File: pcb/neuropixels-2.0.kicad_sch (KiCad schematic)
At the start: 12 parts, among them J2 FH35C-17S-0.3SHW(99), J3 FH35C-17S-0.3SHW(99), U4 STG3856, U5 ECS-2016MV-480-CN-TR

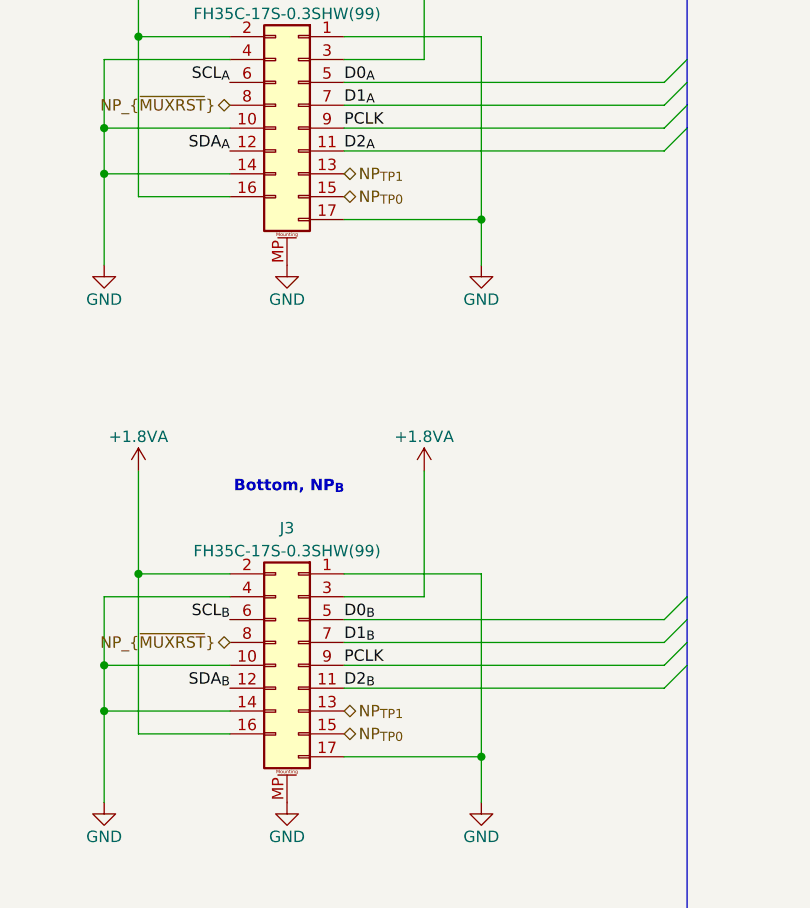
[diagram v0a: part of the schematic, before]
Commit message: Rev. A of public version of headstage
- Being fabricated for testing
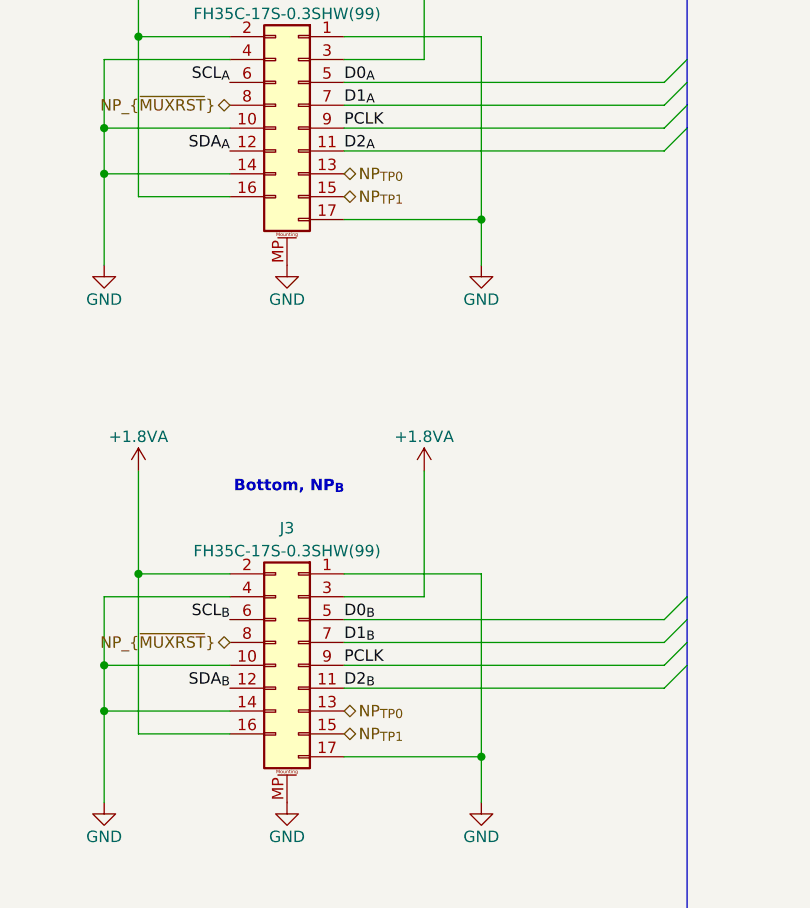
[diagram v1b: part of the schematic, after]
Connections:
- net NP_{TP0}: now also J2.13 (Pin_13), J3.13 (Pin_13); no longer J2.15 (Pin_15), J3.15 (Pin_15)
- net NP_{TP1}: now also J2.15 (Pin_15), J3.15 (Pin_15); no longer J2.13 (Pin_13), J3.13 (Pin_13)
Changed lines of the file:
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@@
   (title_block
     (title "ONIX Neuropixels 2.0 Economical Headstage")
-    (rev "B")
+    (rev "A")
     (company "Open Ephys, Inc")
     (comment 1 "Jonathan P. Newman")
@@
     (effects (font (size 1.27 1.27)) (justify left bottom))
   )
-  (hierarchical_label "NP_{TP1}" (shape bidirectional) (at 176.53 109.22 0) (fields_autoplaced)
+  (hierarchical_label "NP_{TP0}" (shape bidirectional) (at 176.53 49.53 0) (fields_autoplaced)
+    (effects (font (size 1.27 1.27)) (justify left))
+  )
+  (hierarchical_label "NP_{TP1}" (shape bidirectional) (at 176.53 52.07 0) (fields_autoplaced)
     (effects (font (size 1.27 1.27)) (justify left))
   )
   (hierarchical_label "{PSB}" (shape bidirectional) (at 218.44 29.21 0) (fields_autoplaced)
-    (effects (font (size 1.27 1.27)) (justify left))
-  )
-  (hierarchical_label "NP_{TP0}" (shape bidirectional) (at 176.53 111.76 0) (fields_autoplaced)
     (effects (font (size 1.27 1.27)) (justify left))
   )
@@
     (effects (font (size 1.27 1.27)) (justify right))
   )
-  (hierarchical_label "NP_{TP1}" (shape bidirectional) (at 176.53 49.53 0) (fields_autoplaced)
+  (hierarchical_label "NP_{TP1}" (shape bidirectional) (at 176.53 111.76 0) (fields_autoplaced)
     (effects (font (size 1.27 1.27)) (justify left))
   )
@@
     (effects (font (size 1.27 1.27)) (justify right))
   )
-  (hierarchical_label "NP_{TP0}" (shape bidirectional) (at 176.53 52.07 0) (fields_autoplaced)
-    (effects (font (size 1.27 1.27)) (justify left))
-  )
+  (hierarchical_label "NP_{TP0}" (shape bidirectional) (at 176.53 109.22 0) (fields_autoplaced)
+    (effects (font (size 1.27 1.27)) (justify left))
+  )

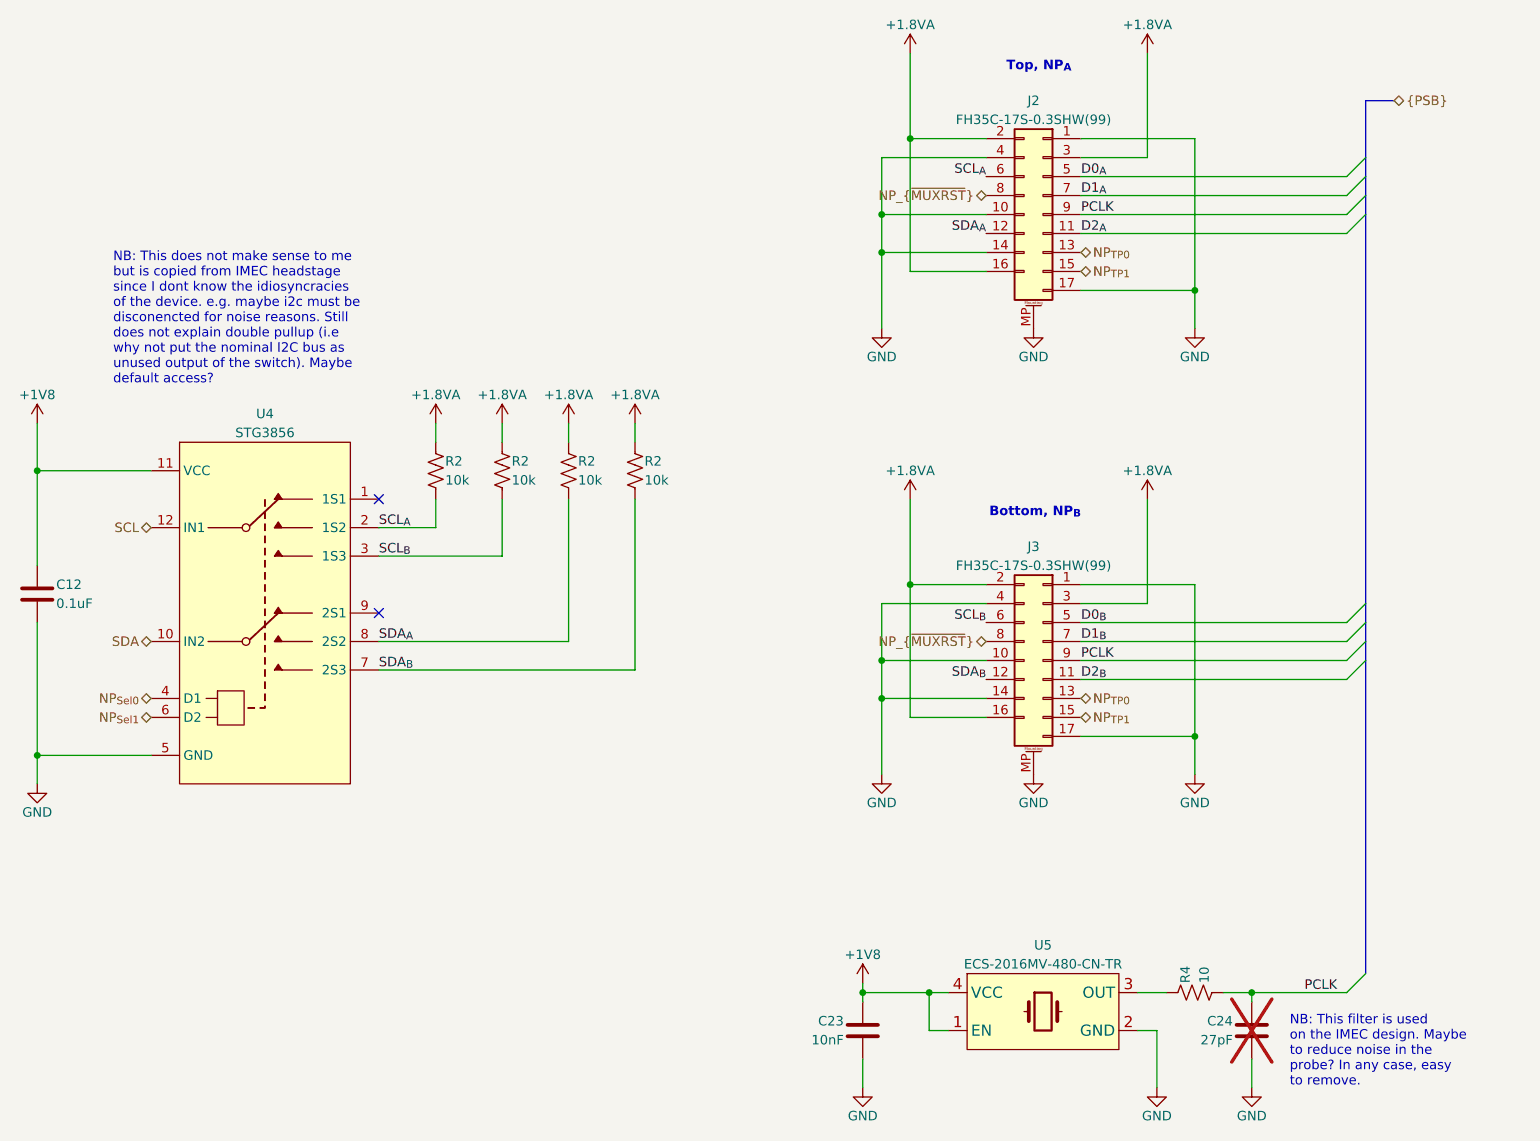
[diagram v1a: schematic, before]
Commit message: Revision B
- Fix incorrect STG3856 symbol and make corresponding changes to PCB
- Flip bits 1 and 2 in probe interaces (fixes #1)
- Improve silkscreen
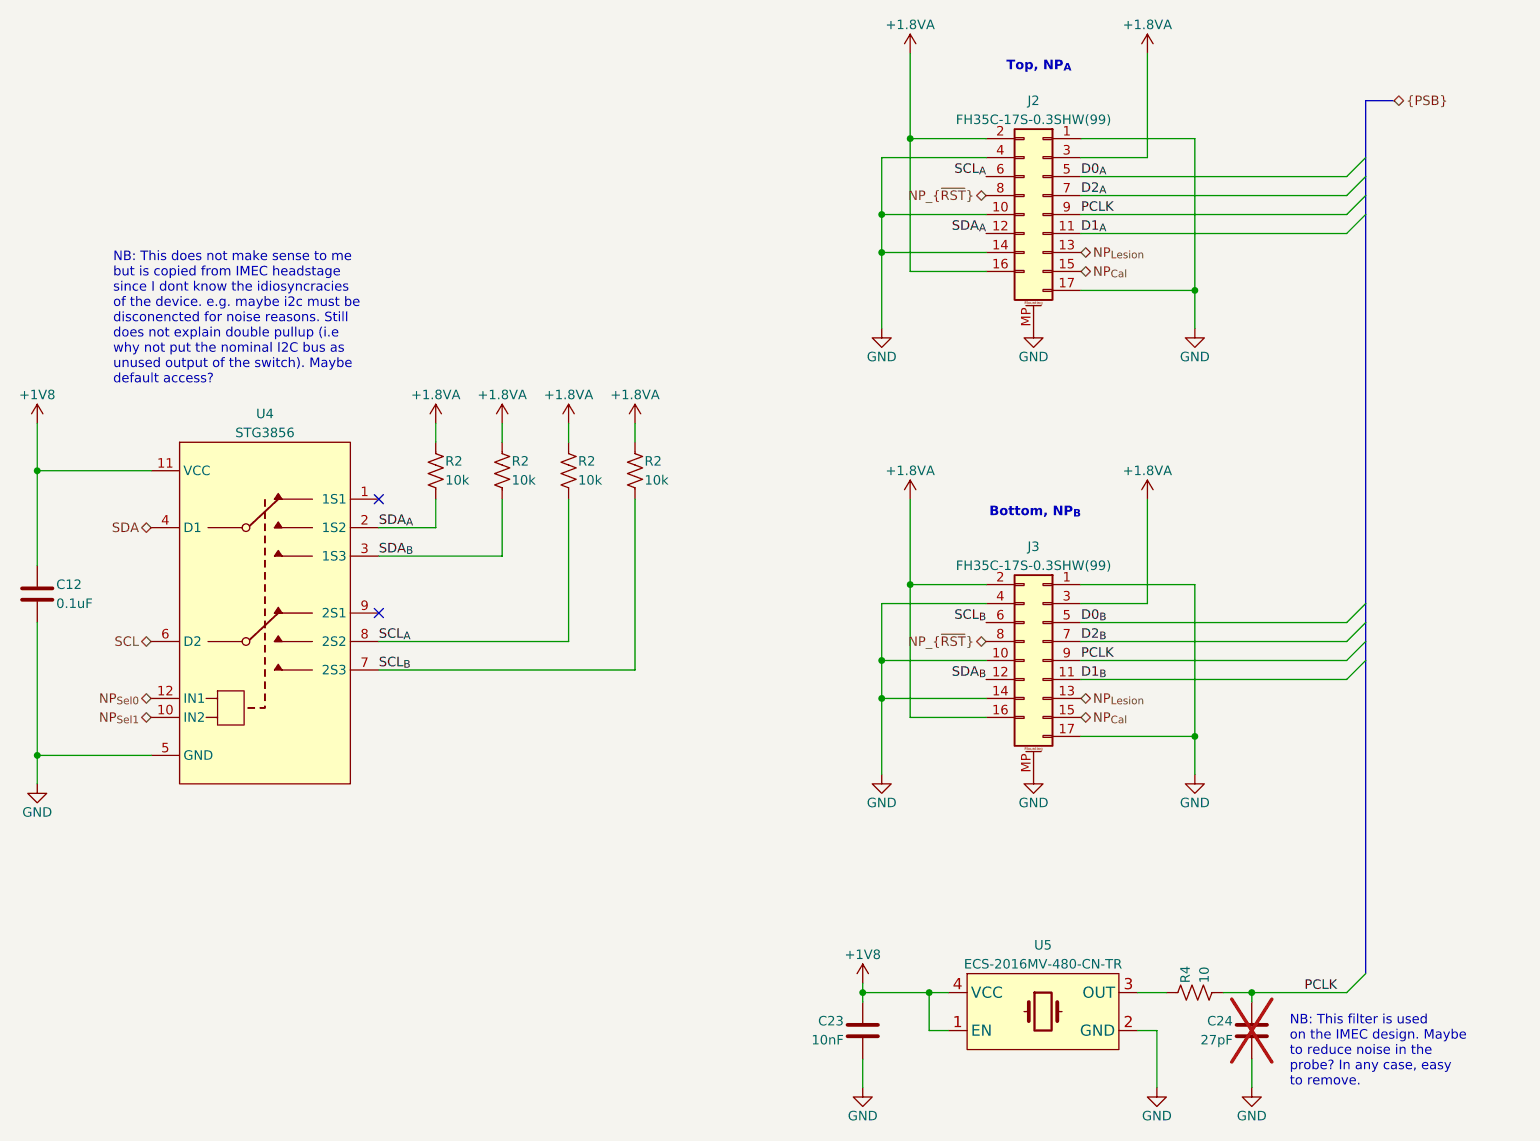
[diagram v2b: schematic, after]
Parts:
- C12, C23, C24, J2, J3, R2, R4, U5: OEPS PN (none) -> ??
- U4: symbol jonnew:STG3856 -> open-ephys:STG3856; OEPS PN (none) -> ??
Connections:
- net D1_{A}: now also J2.11 (Pin_11); no longer J2.7 (Pin_7)
- net D1_{B}: now also J3.11 (Pin_11); no longer J3.7 (Pin_7)
- net D2_{A}: now also J2.7 (Pin_7); no longer J2.11 (Pin_11)
- net D2_{B}: now also J3.7 (Pin_7); no longer J3.11 (Pin_11)
- net NP_{Sel0}: now also U4.12 (IN1); no longer U4.4 (D1)
- net NP_{Sel1}: now also U4.10 (IN2); no longer U4.6 (D2)
- net SCL: now also U4.6 (D2); no longer U4.12 (IN1)
- net SCL_{A}: now also R2.2, U4.8 (2S2); no longer R2.2, U4.2 (1S2)
- net SCL_{B}: now also R2.2, U4.7 (2S3); no longer R2.2, U4.3 (1S3)
- net SDA: now also U4.4 (D1); no longer U4.10 (IN2)
- net SDA_{A}: now also R2.2, U4.2 (1S2); no longer R2.2, U4.8 (2S2)
- net SDA_{B}: now also R2.2, U4.3 (1S3); no longer R2.2, U4.7 (2S3)
- net NP_{TP0} renamed NP_{Lesion}
- net NP_{TP1} renamed NP_{Cal}
- net NP_{~{MUXRST}} renamed NP_{~{RST}}
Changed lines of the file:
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@@
   (title_block
     (title "ONIX Neuropixels 2.0 Economical Headstage")
-    (rev "A")
+    (rev "B")
     (company "Open Ephys, Inc")
     (comment 1 "Jonathan P. Newman")
@@
     (effects (font (size 1.27 1.27)) (justify left bottom))
   )
-  (label "D2_{B}" (at 176.53 106.68 0) (fields_autoplaced)
+  (label "SCL_{A}" (at 82.55 101.6 0) (fields_autoplaced)
     (effects (font (size 1.27 1.27)) (justify left bottom))
   )
-  (label "SCL_{A}" (at 82.55 86.36 0) (fields_autoplaced)
+  (label "D1_{B}" (at 176.53 106.68 0) (fields_autoplaced)
     (effects (font (size 1.27 1.27)) (justify left bottom))
   )
-  (label "SDA_{A}" (at 82.55 101.6 0) (fields_autoplaced)
+  (label "SCL_{B}" (at 82.55 105.41 0) (fields_autoplaced)
     (effects (font (size 1.27 1.27)) (justify left bottom))
   )
@@
     (effects (font (size 1.27 1.27)) (justify left bottom))
   )
+  (label "SDA_{A}" (at 82.55 86.36 0) (fields_autoplaced)
+    (effects (font (size 1.27 1.27)) (justify left bottom))
+  )
   (label "SCL_{A}" (at 163.83 39.37 180) (fields_autoplaced)
     (effects (font (size 1.27 1.27)) (justify right bottom))
@@
     (effects (font (size 1.27 1.27)) (justify left bottom))
   )
-  (label "SCL_{B}" (at 82.55 90.17 0) (fields_autoplaced)
+  (label "SDA_{B}" (at 82.55 90.17 0) (fields_autoplaced)
     (effects (font (size 1.27 1.27)) (justify left bottom))
   )
@@
     (effects (font (size 1.27 1.27)) (justify right bottom))
   )
-  (label "D1_{A}" (at 176.53 41.91 0) (fields_autoplaced)
-    (effects (font (size 1.27 1.27)) (justify left bottom))
-  )
-  (label "SDA_{B}" (at 82.55 105.41 0) (fields_autoplaced)
+  (label "D2_{A}" (at 176.53 41.91 0) (fields_autoplaced)
     (effects (font (size 1.27 1.27)) (justify left bottom))
   )
@@
     (effects (font (size 1.27 1.27)) (justify left bottom))
   )
-  (label "D1_{B}" (at 176.53 101.6 0) (fields_autoplaced)
+  (label "D2_{B}" (at 176.53 101.6 0) (fields_autoplaced)
     (effects (font (size 1.27 1.27)) (justify left bottom))
   )
@@
     (effects (font (size 1.27 1.27)) (justify right bottom))
   )
-  (label "D2_{A}" (at 176.53 46.99 0) (fields_autoplaced)
+  (label "D1_{A}" (at 176.53 46.99 0) (fields_autoplaced)
     (effects (font (size 1.27 1.27)) (justify left bottom))
   )
-  (hierarchical_label "NP_{TP0}" (shape bidirectional) (at 176.53 49.53 0) (fields_autoplaced)
+  (hierarchical_label "NP_{Lesion}" (shape bidirectional) (at 176.53 49.53 0) (fields_autoplaced)
     (effects (font (size 1.27 1.27)) (justify left))
   )
-  (hierarchical_label "NP_{TP1}" (shape bidirectional) (at 176.53 52.07 0) (fields_autoplaced)
+  (hierarchical_label "NP_{Cal}" (shape bidirectional) (at 176.53 52.07 0) (fields_autoplaced)
     (effects (font (size 1.27 1.27)) (justify left))
+  )
+  (hierarchical_label "SCL" (shape bidirectional) (at 52.07 101.6 180) (fields_autoplaced)
+    (effects (font (size 1.27 1.27)) (justify right))
   )
   (hierarchical_label "{PSB}" (shape bidirectional) (at 218.44 29.21 0) (fields_autoplaced)
     (effects (font (size 1.27 1.27)) (justify left))
   )
-  (hierarchical_label "SDA" (shape bidirectional) (at 52.07 101.6 180) (fields_autoplaced)
+  (hierarchical_label "NP_{Cal}" (shape bidirectional) (at 176.53 111.76 0) (fields_autoplaced)
+    (effects (font (size 1.27 1.27)) (justify left))
+  )
+  (hierarchical_label "NP_{~{RST}}" (shape bidirectional) (at 163.83 41.91 180) (fields_autoplaced)
     (effects (font (size 1.27 1.27)) (justify right))
   )
-  (hierarchical_label "NP_{TP1}" (shape bidirectional) (at 176.53 111.76 0) (fields_autoplaced)
+  (hierarchical_label "NP_{Lesion}" (shape bidirectional) (at 176.53 109.22 0) (fields_autoplaced)
     (effects (font (size 1.27 1.27)) (justify left))
   )
-  (hierarchical_label "NP_{~{MUXRST}}" (shape bidirectional) (at 163.83 41.91 180) (fields_autoplaced)
+  (hierarchical_label "SDA" (shape bidirectional) (at 52.07 86.36 180) (fields_autoplaced)
     (effects (font (size 1.27 1.27)) (justify right))
   )
-  (hierarchical_label "SCL" (shape bidirectional) (at 52.07 86.36 180) (fields_autoplaced)
-    (effects (font (size 1.27 1.27)) (justify right))
-  )
-  (hierarchical_label "NP_{TP0}" (shape bidirectional) (at 176.53 109.22 0) (fields_autoplaced)
-    (effects (font (size 1.27 1.27)) (justify left))
-  )
-  (hierarchical_label "NP_{~{MUXRST}}" (shape bidirectional) (at 163.83 101.6 180) (fields_autoplaced)
+  (hierarchical_label "NP_{~{RST}}" (shape bidirectional) (at 163.83 101.6 180) (fields_autoplaced)
     (effects (font (size 1.27 1.27)) (justify right))
   )
@@
     )
   )
-  (symbol (lib_id "jonnew:STG3856") (at 67.31 97.79 0) (unit 1)
+  (symbol (lib_id "open-ephys:STG3856") (at 67.31 97.79 0) (unit 1)
     (in_bom yes) (on_board yes) (dnp no) (fields_autoplaced)
     (property "Reference" "U4" (at 67.31 71.12 0)
@@
     )
     (property "Datasheet" "https://www.st.com/resource/en/datasheet/stg3856.pdf" (at 67.31 97.79 0)
+      (effects (font (size 1.27 1.27)) hide)
+    )
+    (property "OEPS PN" "??" (at 67.31 97.79 0)
       (effects (font (size 1.27 1.27)) hide)
     )
@@
       (effects (font (size 1.27 1.27)) hide)
     )
+    (property "OEPS PN" "??" (at 107.95 78.74 0)
+      (effects (font (size 1.27 1.27)) hide)
+    )
     (pin "1")
     (pin "2")
@@
       (effects (font (size 1.27 1.27)) hide)
     )
+    (property "OEPS PN" "??" (at 191.77 148.59 0)
+      (effects (font (size 1.27 1.27)) hide)
+    )
     (pin "1")
     (pin "2")
@@
     )
     (property "Tolerance" "1%" (at 116.84 78.74 0)
+      (effects (font (size 1.27 1.27)) hide)
+    )
+    (property "OEPS PN" "??" (at 116.84 78.74 0)
       (effects (font (size 1.27 1.27)) hide)
     )
@@
       (effects (font (size 1.27 1.27)) hide)
     )
+    (property "OEPS PN" "??" (at 199.39 153.67 0)
+      (effects (font (size 1.27 1.27)) hide)
+    )
     (pin "1")
     (pin "2")
@@
     )
     (property "Tolerance" "" (at 147.32 153.67 0)
+      (effects (font (size 1.27 1.27)) hide)
+    )
+    (property "OEPS PN" "??" (at 147.32 153.67 0)
       (effects (font (size 1.27 1.27)) hide)
     )
@@
       (effects (font (size 1.27 1.27)) hide)
     )
+    (property "OEPS PN" "??" (at 99.06 78.74 0)
+      (effects (font (size 1.27 1.27)) hide)
+    )
     (pin "1")
     (pin "2")
@@
       (effects (font (size 1.27 1.27)) hide)
     )
+    (property "OEPS PN" "??" (at 90.17 78.74 0)
+      (effects (font (size 1.27 1.27)) hide)
+    )
     (pin "1")
     (pin "2")
@@
     )
     (property "Tolerance" "" (at 36.83 95.25 0)
+      (effects (font (size 1.27 1.27)) hide)
+    )
+    (property "OEPS PN" "??" (at 36.83 95.25 0)
       (effects (font (size 1.27 1.27)) hide)
     )
@@
     )
     (property "Datasheet" "https://www.mouser.com/datasheet/2/185/FH35C_17S_0_3SHW_99__CL0580_2916_1_99_2DDrawing_00-1615065.pdf" (at 171.45 104.14 0)
+      (effects (font (size 1.27 1.27)) hide)
+    )
+    (property "OEPS PN" "??" (at 171.45 104.14 0)
       (effects (font (size 1.27 1.27)) hide)
     )
@@
       (effects (font (size 1.27 1.27)) hide)
     )
+    (property "OEPS PN" "??" (at 171.45 151.13 0)
+      (effects (font (size 1.27 1.27)) hide)
+    )
     (pin "1")
     (pin "2")
@@
       (effects (font (size 1.27 1.27)) hide)
     )
+    (property "OEPS PN" "??" (at 171.45 44.45 0)
+      (effects (font (size 1.27 1.27)) hide)
+    )
